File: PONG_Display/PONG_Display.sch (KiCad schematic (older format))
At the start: 0 parts

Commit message: V2
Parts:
- added FID? (x4): Fiducial, symbol Mechanical:Fiducial
- added H? (x4): MountingHole, symbol Mechanical:MountingHole
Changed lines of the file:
@@
 $Descr A4 11693 8268
 encoding utf-8
-Sheet 1 7
+Sheet 1 6
 Title ""
 Date ""
@@
 $EndDescr
 $Sheet
-S 8000 1500 1350 1500
+S 8400 1950 1350 1500
 U 5E80B1F8
 F0 "Moduł WiFi" 50
 F1 "esp.sch" 50
-$EndSheet
-$Sheet
-S 5000 4450 2900 1250
+F2 "GND" I L 8400 3250 50
+F3 "+3.3V" I L 8400 2150 50
+F4 "ESP_RX" B L 8400 2350 50
+F5 "ESP_TX" B L 8400 2500 50
+F6 "ESP_GPIO0" B L 8400 2650 50
+F7 "ESP_GPIO2" B L 8400 2800 50
+F8 "ESP_RST" I L 8400 2950 50
+F9 "ESP_CH_PD" I L 8400 3100 50
+$EndSheet
+$Sheet
+S 2650 1950 1200 1200
+U 5E80B6DE
+F0 "Sensory" 50
+F1 "sensors.sch" 50
+F2 "LIGHT_SENSOR_IN" I R 3850 2350 50
+F3 "LIGHT_SENSO_OUT" O R 3850 2500 50
+F4 "+5V" I L 2650 2200 50
+F5 "+3.3V" I L 2650 2300 50
+F6 "GND" I L 2650 2900 50
+F7 "DHT22_DATA" O R 3850 2650 50
+F8 "PIR_OUT" O R 3850 2800 50
+$EndSheet
+$Sheet
+S 8800 4400 900  1250
+U 5E80C133
+F0 "Wyswietlacz LED" 50
+F1 "LED.sch" 50
+F2 "+12V" I L 8800 4500 50
+F3 "GND" I L 8800 5400 50
+F4 "LED_DATA" I L 8800 4900 50
+$EndSheet
+$Sheet
+S 5400 1900 1800 1500
+U 5E80B18F
+F0 "MikrokontrolerAtmega" 50
+F1 "microcontroler.sch" 50
+F2 "+5V" I L 5400 2150 50
+F3 "GND" I L 5400 3200 50
+F4 "LIGHT_SENSOR_OUT" I L 5400 2500 50
+F5 "ESP_RX" B R 7200 2350 50
+F6 "ESP_TX" B R 7200 2500 50
+F7 "LIGHT_SENSOR_IN" O L 5400 2350 50
+F8 "ESP_GPIO0" B R 7200 2650 50
+F9 "ESP_GPIO2" B R 7200 2800 50
+F10 "PIR_OUT" I L 5400 2800 50
+F11 "DHT22_DATA" I L 5400 2650 50
+F12 "LED_DATA" O R 7200 3050 50
+$EndSheet
+$Sheet
+S 1750 4350 1100 1150
 U 5E80B14C
 F0 "Power Supply" 50
 F1 "Power_supply.sch" 50
-$EndSheet
-$Sheet
-S 2250 1500 1350 1500
-U 5E80B6DE
-F0 "Sensory" 50
-F1 "sensors.sch" 50
-$EndSheet
-$Sheet
-S 2150 3950 1750 2350
-U 5E80C133
-F0 "Wyswietlacz LED" 50
-F1 "LED.sch" 50
-$EndSheet
-$Sheet
-S 5000 1450 1800 1500
-U 5E80B18F
-F0 "MikrokontrolerAtmega" 50
-F1 "microcontroler.sch" 50
-$EndSheet
-$Sheet
-S 9200 4350 1150 1350
-U 5E80CCDD
-F0 "Interfejs złączy" 50
-F1 "IOinterface.sch" 50
-$EndSheet
+F2 "+5V" O R 2850 4650 50
+F3 "GND" O R 2850 5400 50
+F4 "+3V" O R 2850 4800 50
+F5 "+12V" O R 2850 4500 50
+$EndSheet
+Wire Wire Line
+	7200 2350 8400 2350
+Wire Wire Line
+	7200 2500 8400 2500
+Wire Wire Line
+	7200 2650 8400 2650
+Wire Wire Line
+	7200 2800 8400 2800
+Wire Wire Line
+	3850 2350 5400 2350
+Wire Wire Line
+	5400 2500 3850 2500
+Wire Wire Line
+	3850 2650 5400 2650
+Wire Wire Line
+	5400 2800 3850 2800
+Wire Wire Line
+	2850 5400 3350 5400
+Wire Wire Line
+	3150 4650 3150 3850
+Wire Wire Line
+	3150 3850 2000 3850
+Wire Wire Line
+	2000 3850 2000 2200
+Wire Wire Line
+	2000 2200 2650 2200
+Wire Wire Line
+	2850 4800 3250 4800
+Wire Wire Line
+	3250 4800 3250 3750
+Wire Wire Line
+	3250 3750 2100 3750
+Wire Wire Line
+	2100 3750 2100 2300
+Wire Wire Line
+	2100 2300 2650 2300
+Wire Wire Line
+	3350 5400 3350 3650
+Wire Wire Line
+	3350 3650 2200 3650
+Wire Wire Line
+	2200 3650 2200 2900
+Wire Wire Line
+	2200 2900 2650 2900
+Connection ~ 3350 5400
+Wire Wire Line
+	3350 5400 5050 5400
+Wire Wire Line
+	2850 4650 3150 4650
+Wire Wire Line
+	3150 4650 4950 4650
+Wire Wire Line
+	4950 4650 4950 2150
+Wire Wire Line
+	4950 2150 5400 2150
+Connection ~ 3150 4650
+Wire Wire Line
+	5400 3200 5050 3200
+Wire Wire Line
+	5050 3200 5050 5400
+Connection ~ 5050 5400
+Wire Wire Line
+	8400 3250 8100 3250
+Wire Wire Line
+	8100 3250 8100 5400
+Wire Wire Line
+	8400 2150 7900 2150
+Wire Wire Line
+	7900 2150 7900 4800
+Wire Wire Line
+	7900 4800 3250 4800
+Connection ~ 3250 4800
+Wire Wire Line
+	5050 5400 8100 5400
+Connection ~ 8100 5400
+Wire Wire Line
+	2850 4500 8800 4500
+Wire Wire Line
+	8100 5400 8800 5400
+Wire Wire Line
+	7200 3050 8000 3050
+Wire Wire Line
+	8000 3050 8000 4900
+Wire Wire Line
+	8000 4900 8800 4900
+$Comp
+L Mechanical:Fiducial FID?
+U 1 1 5E8DB9CF
+P 1350 6100
+AR Path="/5E80B18F/5E8DB9CF" Ref="FID?"  Part="1"
+AR Path="/5E8DB9CF" Ref="FID?"  Part="1"
+F 0 "FID?" H 1435 6146 50  0000 L CNN
+F 1 "Fiducial" H 1435 6055 50  0000 L CNN
+F 2 "" H 1350 6100 50  0001 C CNN
+F 3 "~" H 1350 6100 50  0001 C CNN
+	1    1350 6100
+	1    0    0    -1
+$EndComp
+$Comp
+L Mechanical:Fiducial FID?
+U 1 1 5E8DB9D5
+P 1350 6500
+AR Path="/5E80B18F/5E8DB9D5" Ref="FID?"  Part="1"
+AR Path="/5E8DB9D5" Ref="FID?"  Part="1"
+F 0 "FID?" H 1435 6546 50  0000 L CNN
+F 1 "Fiducial" H 1435 6455 50  0000 L CNN
+F 2 "" H 1350 6500 50  0001 C CNN
+F 3 "~" H 1350 6500 50  0001 C CNN
+	1    1350 6500
+	1    0    0    -1
+$EndComp
+$Comp
+L Mechanical:Fiducial FID?
+U 1 1 5E8DB9DB
+P 1350 6900
+AR Path="/5E80B18F/5E8DB9DB" Ref="FID?"  Part="1"
+AR Path="/5E8DB9DB" Ref="FID?"  Part="1"
+F 0 "FID?" H 1435 6946 50  0000 L CNN
+F 1 "Fiducial" H 1435 6855 50  0000 L CNN
+F 2 "" H 1350 6900 50  0001 C CNN
+F 3 "~" H 1350 6900 50  0001 C CNN
+	1    1350 6900
+	1    0    0    -1
+$EndComp
+$Comp
+L Mechanical:Fiducial FID?
+U 1 1 5E8DB9E1
+P 1350 7250
+AR Path="/5E80B18F/5E8DB9E1" Ref="FID?"  Part="1"
+AR Path="/5E8DB9E1" Ref="FID?"  Part="1"
+F 0 "FID?" H 1435 7296 50  0000 L CNN
+F 1 "Fiducial" H 1435 7205 50  0000 L CNN
+F 2 "" H 1350 7250 50  0001 C CNN
+F 3 "~" H 1350 7250 50  0001 C CNN
+	1    1350 7250
+	1    0    0    -1
+$EndComp
+$Comp
+L Mechanical:MountingHole H?
+U 1 1 5E8DB9E7
+P 2250 6100
+AR Path="/5E80B18F/5E8DB9E7" Ref="H?"  Part="1"
+AR Path="/5E8DB9E7" Ref="H?"  Part="1"
+F 0 "H?" H 2350 6146 50  0000 L CNN
+F 1 "MountingHole" H 2350 6055 50  0000 L CNN
+F 2 "" H 2250 6100 50  0001 C CNN
+F 3 "~" H 2250 6100 50  0001 C CNN
+	1    2250 6100
+	1    0    0    -1
+$EndComp
+$Comp
+L Mechanical:MountingHole H?
+U 1 1 5E8DB9ED
+P 2250 6550
+AR Path="/5E80B18F/5E8DB9ED" Ref="H?"  Part="1"
+AR Path="/5E8DB9ED" Ref="H?"  Part="1"
+F 0 "H?" H 2350 6596 50  0000 L CNN
+F 1 "MountingHole" H 2350 6505 50  0000 L CNN
+F 2 "" H 2250 6550 50  0001 C CNN
+F 3 "~" H 2250 6550 50  0001 C CNN
+	1    2250 6550
+	1    0    0    -1
+$EndComp
+$Comp
+L Mechanical:MountingHole H?
+U 1 1 5E8DB9F3
+P 2250 6950
+AR Path="/5E80B18F/5E8DB9F3" Ref="H?"  Part="1"
+AR Path="/5E8DB9F3" Ref="H?"  Part="1"
+F 0 "H?" H 2350 6996 50  0000 L CNN
+F 1 "MountingHole" H 2350 6905 50  0000 L CNN
+F 2 "" H 2250 6950 50  0001 C CNN
+F 3 "~" H 2250 6950 50  0001 C CNN
+	1    2250 6950
+	1    0    0    -1
+$EndComp
+$Comp
+L Mechanical:MountingHole H?
+U 1 1 5E8DB9F9
+P 2250 7350
+AR Path="/5E80B18F/5E8DB9F9" Ref="H?"  Part="1"
+AR Path="/5E8DB9F9" Ref="H?"  Part="1"
+F 0 "H?" H 2350 7396 50  0000 L CNN
+F 1 "MountingHole" H 2350 7305 50  0000 L CNN
+F 2 "" H 2250 7350 50  0001 C CNN
+F 3 "~" H 2250 7350 50  0001 C CNN
+	1    2250 7350
+	1    0    0    -1
+$EndComp
 $EndSCHEMATC

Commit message: V3
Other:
- note added: "Wyświetlacz ping-pong - schemat główny"

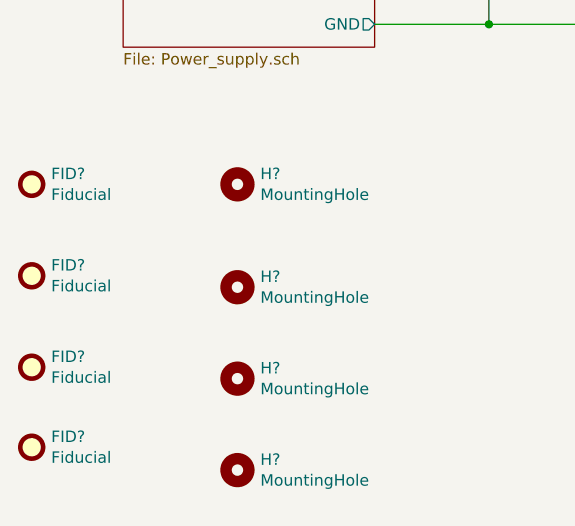
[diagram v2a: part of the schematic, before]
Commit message: Dodane footprinty
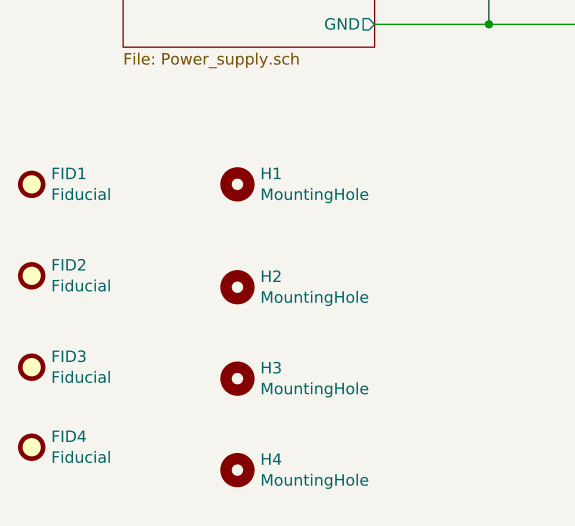
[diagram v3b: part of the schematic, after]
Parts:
- FID1, FID2, FID3, FID4: renamed from FID?; footprint (none) -> Fiducial:Fiducial_0.5mm_Mask1.5mm
- H1, H2, H3, H4: renamed from H?; footprint (none) -> MountingHole:MountingHole_2.7mm_Pad_Via
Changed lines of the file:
@@
 P 1350 6100
 AR Path="/5E80B18F/5E8DB9CF" Ref="FID?"  Part="1"
-AR Path="/5E8DB9CF" Ref="FID?"  Part="1"
-F 0 "FID?" H 1435 6146 50  0000 L CNN
+AR Path="/5E8DB9CF" Ref="FID1"  Part="1"
+F 0 "FID1" H 1435 6146 50  0000 L CNN
 F 1 "Fiducial" H 1435 6055 50  0000 L CNN
-F 2 "" H 1350 6100 50  0001 C CNN
+F 2 "Fiducial:Fiducial_0.5mm_Mask1.5mm" H 1350 6100 50  0001 C CNN
 F 3 "~" H 1350 6100 50  0001 C CNN
 	1    1350 6100
@@
 P 1350 6500
 AR Path="/5E80B18F/5E8DB9D5" Ref="FID?"  Part="1"
-AR Path="/5E8DB9D5" Ref="FID?"  Part="1"
-F 0 "FID?" H 1435 6546 50  0000 L CNN
+AR Path="/5E8DB9D5" Ref="FID2"  Part="1"
+F 0 "FID2" H 1435 6546 50  0000 L CNN
 F 1 "Fiducial" H 1435 6455 50  0000 L CNN
-F 2 "" H 1350 6500 50  0001 C CNN
+F 2 "Fiducial:Fiducial_0.5mm_Mask1.5mm" H 1350 6500 50  0001 C CNN
 F 3 "~" H 1350 6500 50  0001 C CNN
 	1    1350 6500
@@
 P 1350 6900
 AR Path="/5E80B18F/5E8DB9DB" Ref="FID?"  Part="1"
-AR Path="/5E8DB9DB" Ref="FID?"  Part="1"
-F 0 "FID?" H 1435 6946 50  0000 L CNN
+AR Path="/5E8DB9DB" Ref="FID3"  Part="1"
+F 0 "FID3" H 1435 6946 50  0000 L CNN
 F 1 "Fiducial" H 1435 6855 50  0000 L CNN
-F 2 "" H 1350 6900 50  0001 C CNN
+F 2 "Fiducial:Fiducial_0.5mm_Mask1.5mm" H 1350 6900 50  0001 C CNN
 F 3 "~" H 1350 6900 50  0001 C CNN
 	1    1350 6900
@@
 P 1350 7250
 AR Path="/5E80B18F/5E8DB9E1" Ref="FID?"  Part="1"
-AR Path="/5E8DB9E1" Ref="FID?"  Part="1"
-F 0 "FID?" H 1435 7296 50  0000 L CNN
+AR Path="/5E8DB9E1" Ref="FID4"  Part="1"
+F 0 "FID4" H 1435 7296 50  0000 L CNN
 F 1 "Fiducial" H 1435 7205 50  0000 L CNN
-F 2 "" H 1350 7250 50  0001 C CNN
+F 2 "Fiducial:Fiducial_0.5mm_Mask1.5mm" H 1350 7250 50  0001 C CNN
 F 3 "~" H 1350 7250 50  0001 C CNN
 	1    1350 7250
@@
 P 2250 6100
 AR Path="/5E80B18F/5E8DB9E7" Ref="H?"  Part="1"
-AR Path="/5E8DB9E7" Ref="H?"  Part="1"
-F 0 "H?" H 2350 6146 50  0000 L CNN
+AR Path="/5E8DB9E7" Ref="H1"  Part="1"
+F 0 "H1" H 2350 6146 50  0000 L CNN
 F 1 "MountingHole" H 2350 6055 50  0000 L CNN
-F 2 "" H 2250 6100 50  0001 C CNN
+F 2 "MountingHole:MountingHole_2.7mm_Pad_Via" H 2250 6100 50  0001 C CNN
 F 3 "~" H 2250 6100 50  0001 C CNN
 	1    2250 6100
@@
 P 2250 6550
 AR Path="/5E80B18F/5E8DB9ED" Ref="H?"  Part="1"
-AR Path="/5E8DB9ED" Ref="H?"  Part="1"
-F 0 "H?" H 2350 6596 50  0000 L CNN
+AR Path="/5E8DB9ED" Ref="H2"  Part="1"
+F 0 "H2" H 2350 6596 50  0000 L CNN
 F 1 "MountingHole" H 2350 6505 50  0000 L CNN
-F 2 "" H 2250 6550 50  0001 C CNN
+F 2 "MountingHole:MountingHole_2.7mm_Pad_Via" H 2250 6550 50  0001 C CNN
 F 3 "~" H 2250 6550 50  0001 C CNN
 	1    2250 6550
@@
 P 2250 6950
 AR Path="/5E80B18F/5E8DB9F3" Ref="H?"  Part="1"
-AR Path="/5E8DB9F3" Ref="H?"  Part="1"
-F 0 "H?" H 2350 6996 50  0000 L CNN
+AR Path="/5E8DB9F3" Ref="H3"  Part="1"
+F 0 "H3" H 2350 6996 50  0000 L CNN
 F 1 "MountingHole" H 2350 6905 50  0000 L CNN
-F 2 "" H 2250 6950 50  0001 C CNN
+F 2 "MountingHole:MountingHole_2.7mm_Pad_Via" H 2250 6950 50  0001 C CNN
 F 3 "~" H 2250 6950 50  0001 C CNN
 	1    2250 6950
@@
 P 2250 7350
 AR Path="/5E80B18F/5E8DB9F9" Ref="H?"  Part="1"
-AR Path="/5E8DB9F9" Ref="H?"  Part="1"
-F 0 "H?" H 2350 7396 50  0000 L CNN
+AR Path="/5E8DB9F9" Ref="H4"  Part="1"
+F 0 "H4" H 2350 7396 50  0000 L CNN
 F 1 "MountingHole" H 2350 7305 50  0000 L CNN
-F 2 "" H 2250 7350 50  0001 C CNN
+F 2 "MountingHole:MountingHole_2.7mm_Pad_Via" H 2250 7350 50  0001 C CNN
 F 3 "~" H 2250 7350 50  0001 C CNN
 	1    2250 7350

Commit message: napisałem coś
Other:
- note added: "Ja tu byłem"
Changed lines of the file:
@@
 EESchema Schematic File Version 4
+LIBS:PONG_Display-cache
 EELAYER 30 0
 EELAYER END
@@
 Text Notes 7600 7500 0    50   ~ 0
 Wyświetlacz ping-pong - schemat główny
+Text Notes 5450 1100 0    50   ~ 0
+Ja tu byłem
 $EndSCHEMATC

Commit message: poprawka
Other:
- note removed: "Ja tu byłem"
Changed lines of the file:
@@
 EESchema Schematic File Version 4
-LIBS:PONG_Display-cache
 EELAYER 30 0
 EELAYER END
@@
 Text Notes 7600 7500 0    50   ~ 0
 Wyświetlacz ping-pong - schemat główny
-Text Notes 5450 1100 0    50   ~ 0
-Ja tu byłem
 $EndSCHEMATC

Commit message: Drobne zmiany
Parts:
- removed FID1, FID2, FID3, FID4: Fiducial, Fiducial:Fiducial_0.5mm_Mask1.5mm, symbol Mechanical:Fiducial
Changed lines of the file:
@@
 	8000 4900 8800 4900
-$Comp
-L Mechanical:Fiducial FID?
-U 1 1 5E8DB9CF
-P 1350 6100
-AR Path="/5E80B18F/5E8DB9CF" Ref="FID?"  Part="1"
-AR Path="/5E8DB9CF" Ref="FID1"  Part="1"
-F 0 "FID1" H 1435 6146 50  0000 L CNN
-F 1 "Fiducial" H 1435 6055 50  0000 L CNN
-F 2 "Fiducial:Fiducial_0.5mm_Mask1.5mm" H 1350 6100 50  0001 C CNN
-F 3 "~" H 1350 6100 50  0001 C CNN
-	1    1350 6100
-	1    0    0    -1
-$EndComp
-$Comp
-L Mechanical:Fiducial FID?
-U 1 1 5E8DB9D5
-P 1350 6500
-AR Path="/5E80B18F/5E8DB9D5" Ref="FID?"  Part="1"
-AR Path="/5E8DB9D5" Ref="FID2"  Part="1"
-F 0 "FID2" H 1435 6546 50  0000 L CNN
-F 1 "Fiducial" H 1435 6455 50  0000 L CNN
-F 2 "Fiducial:Fiducial_0.5mm_Mask1.5mm" H 1350 6500 50  0001 C CNN
-F 3 "~" H 1350 6500 50  0001 C CNN
-	1    1350 6500
-	1    0    0    -1
-$EndComp
-$Comp
-L Mechanical:Fiducial FID?
-U 1 1 5E8DB9DB
-P 1350 6900
-AR Path="/5E80B18F/5E8DB9DB" Ref="FID?"  Part="1"
-AR Path="/5E8DB9DB" Ref="FID3"  Part="1"
-F 0 "FID3" H 1435 6946 50  0000 L CNN
-F 1 "Fiducial" H 1435 6855 50  0000 L CNN
-F 2 "Fiducial:Fiducial_0.5mm_Mask1.5mm" H 1350 6900 50  0001 C CNN
-F 3 "~" H 1350 6900 50  0001 C CNN
-	1    1350 6900
-	1    0    0    -1
-$EndComp
-$Comp
-L Mechanical:Fiducial FID?
-U 1 1 5E8DB9E1
-P 1350 7250
-AR Path="/5E80B18F/5E8DB9E1" Ref="FID?"  Part="1"
-AR Path="/5E8DB9E1" Ref="FID4"  Part="1"
-F 0 "FID4" H 1435 7296 50  0000 L CNN
-F 1 "Fiducial" H 1435 7205 50  0000 L CNN
-F 2 "Fiducial:Fiducial_0.5mm_Mask1.5mm" H 1350 7250 50  0001 C CNN
-F 3 "~" H 1350 7250 50  0001 C CNN
-	1    1350 7250
-	1    0    0    -1
-$EndComp
 $Comp
 L Mechanical:MountingHole H?

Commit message: Teraz jest sexy
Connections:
- wire segments 39 -> 11
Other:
- note added: "1)Nie przypisany LED_DATA\n\n2)Poziomy logiczne TX i RX\n\n3)Jakie GPIO z klocka \n\n4)Czy pot do przetwornicy\n\n5)5,6,21 pin Atmegi\n\n6)RTC może brać 5V\n\n7)RTC sprawdzić\n\n8)Przypisać piny ESP\n\n9)Reset klocka i ESP ten sam?\n\n10)Omówić klocek\n\n11)Reset ESP\n\n12)Programator ESP\n"
- note added: "To do:\n"
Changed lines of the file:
@@
 EESchema Schematic File Version 4
+LIBS:PONG_Display-cache
 EELAYER 30 0
 EELAYER END
@@
 F0 "Wyswietlacz LED" 50
 F1 "LED.sch" 50
-F2 "+12V" I L 8800 4500 50
-F3 "GND" I L 8800 5400 50
-F4 "LED_DATA" I L 8800 4900 50
+F2 "LED_DATA" I L 8800 4900 50
 $EndSheet
 $Sheet
-S 1750 4350 1100 1150
+S 2650 4050 1100 1150
 U 5E80B14C
 F0 "Power Supply" 50
 F1 "Power_supply.sch" 50
-F2 "+5V" O R 2850 4650 50
-F3 "GND" O R 2850 5400 50
-F4 "+3V" O R 2850 4800 50
-F5 "+12V" O R 2850 4500 50
 $EndSheet
 Wire Wire Line
@@
 Wire Wire Line
 	5400 2800 3850 2800
-Wire Wire Line
-	2850 5400 3350 5400
-Wire Wire Line
-	3150 4650 3150 3850
-Wire Wire Line
-	3150 3850 2000 3850
-Wire Wire Line
-	2000 3850 2000 2200
-Wire Wire Line
-	2000 2200 2650 2200
-Wire Wire Line
-	2850 4800 3250 4800
-Wire Wire Line
-	3250 4800 3250 3750
-Wire Wire Line
-	3250 3750 2100 3750
-Wire Wire Line
-	2100 3750 2100 2300
-Wire Wire Line
-	2100 2300 2650 2300
-Wire Wire Line
-	3350 5400 3350 3650
-Wire Wire Line
-	3350 3650 2200 3650
-Wire Wire Line
-	2200 3650 2200 2900
-Wire Wire Line
-	2200 2900 2650 2900
-Connection ~ 3350 5400
-Wire Wire Line
-	3350 5400 5050 5400
-Wire Wire Line
-	2850 4650 3150 4650
-Wire Wire Line
-	3150 4650 4950 4650
-Wire Wire Line
-	4950 4650 4950 2150
-Wire Wire Line
-	4950 2150 5400 2150
-Connection ~ 3150 4650
-Wire Wire Line
-	5400 3200 5050 3200
-Wire Wire Line
-	5050 3200 5050 5400
-Connection ~ 5050 5400
-Wire Wire Line
-	8400 3300 8100 3300
-Wire Wire Line
-	8100 3300 8100 5400
-Wire Wire Line
-	8400 2150 7900 2150
-Wire Wire Line
-	7900 2150 7900 4800
-Wire Wire Line
-	7900 4800 3250 4800
-Connection ~ 3250 4800
-Wire Wire Line
-	5050 5400 8100 5400
-Connection ~ 8100 5400
-Wire Wire Line
-	2850 4500 8800 4500
-Wire Wire Line
-	8100 5400 8800 5400
 Wire Wire Line
 	7200 3300 8000 3300
@@
 	1    0    0    -1
 $EndComp
+Wire Wire Line
+	5400 2500 3850 2500
+Text Notes 7600 7500 0    50   ~ 0
+Wyświetlacz ping-pong - schemat główny
 $Sheet
 S 2650 1950 1200 1200
@@
 F0 "Sensory" 50
 F1 "sensors.sch" 50
-F2 "LIGHT_SENSO_OUT" O R 3850 2500 50
-F3 "+5V" I L 2650 2200 50
-F4 "+3.3V" I L 2650 2300 50
-F5 "GND" I L 2650 2900 50
-F6 "DHT22_DATA" O R 3850 2650 50
-F7 "PIR_OUT" O R 3850 2800 50
+F2 "DHT22_DATA" I R 3850 2650 50
+F3 "LIGHT_SENSOR_OUT" I R 3850 2500 50
+F4 "PIR_OUT" I R 3850 2800 50
 $EndSheet
-Wire Wire Line
-	5400 2500 3850 2500
 $Sheet
 S 5400 1900 1800 1500
@@
 F0 "MikrokontrolerAtmega" 50
 F1 "microcontroler.sch" 50
-F2 "+5V" I L 5400 2150 50
-F3 "GND" I L 5400 3200 50
-F4 "LIGHT_SENSOR_OUT" I L 5400 2500 50
-F5 "ESP_RX" B R 7200 2350 50
-F6 "ESP_TX" B R 7200 2500 50
-F7 "ESP_GPIO0" B R 7200 2650 50
-F8 "ESP_GPIO2" B R 7200 2800 50
-F9 "PIR_OUT" I L 5400 2800 50
-F10 "DHT22_DATA" I L 5400 2650 50
-F11 "LED_DATA" O R 7200 3300 50
+F2 "LIGHT_SENSOR_OUT" I L 5400 2500 50
+F3 "PIR_SENSOR_OUT" I L 5400 2800 50
+F4 "DHT22_DATA" I L 5400 2650 50
+F5 "ESP_TX" I R 7200 2500 50
+F6 "ESP_RX" I R 7200 2350 50
+F7 "ESP_RST" I R 7200 2950 50
 $EndSheet
+Wire Wire Line
+	7200 2950 8400 2950
 $Sheet
 S 8400 1950 1350 1500
@@
 F0 "Moduł WiFi" 50
 F1 "esp.sch" 50
-F2 "GND" I L 8400 3300 50
-F3 "+3.3V" I L 8400 2150 50
-F4 "ESP_RX" B L 8400 2350 50
-F5 "ESP_TX" B L 8400 2500 50
-F6 "ESP_GPIO0" B L 8400 2650 50
-F7 "ESP_GPIO2" B L 8400 2800 50
-F8 "ESP_RST" I L 8400 2950 50
-F9 "ESP_CH_PD" I L 8400 3100 50
+F2 "ESP_RX" I L 8400 2350 50
+F3 "ESP_TX" I L 8400 2500 50
+F4 "ESP_RST" I L 8400 2950 50
+F5 "ESP_CH_PD" I L 8400 3100 50
+F6 "ESP_GPIO0" I L 8400 2650 50
+F7 "ESP_GPIO2" I L 8400 2800 50
 $EndSheet
-Text Notes 7600 7500 0    50   ~ 0
-Wyświetlacz ping-pong - schemat główny
+Text Notes 950  1150 0    197  Italic 39
+To do:\n
+Text Notes 700  4350 0    79   ~ 0
+1)Nie przypisany LED_DATA\n\n2)Poziomy logiczne TX i RX\n\n3)Jakie GPIO z klocka \n\n4)Czy pot do przetwornicy\n\n5)5,6,21 pin Atmegi\n\n6)RTC może brać 5V\n\n7)RTC sprawdzić\n\n8)Przypisać piny ESP\n\n9)Reset klocka i ESP ten sam?\n\n10)Omówić klocek\n\n11)Reset ESP\n\n12)Programator ESP\n
 $EndSCHEMATC

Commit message: 2
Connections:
- wire segments 11 -> 9
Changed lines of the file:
@@
 EESchema Schematic File Version 4
-LIBS:PONG_Display-cache
 EELAYER 30 0
 EELAYER END
@@
 Wire Wire Line
 	7200 2500 8400 2500
-Wire Wire Line
-	7200 2650 8400 2650
-Wire Wire Line
-	7200 2800 8400 2800
 Wire Wire Line
 	3850 2650 5400 2650
@@
 F6 "ESP_RX" I R 7200 2350 50
 F7 "ESP_RST" I R 7200 2950 50
+F8 "LED_DATA" I R 7200 3300 50
 $EndSheet
 Wire Wire Line
